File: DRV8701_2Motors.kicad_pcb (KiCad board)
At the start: 4 copper layers, 100 x 40 mm, 92 parts, among them J1 Conn_01x02, J10 Conn_01x04, J11 Conn_01x03, J2 Conn_01x10, J3 Conn_01x10, J4 Conn_01x02, J5 Conn_01x02, J6 Conn_01x04, J7 Conn_ST_STDC14, J8 Conn_01x03, J9 Conn_01x04, SW1 SW_SPDT_321, U16 STM32F303RETx, U3 AM26LV32xD, U4 AM26LV32xD

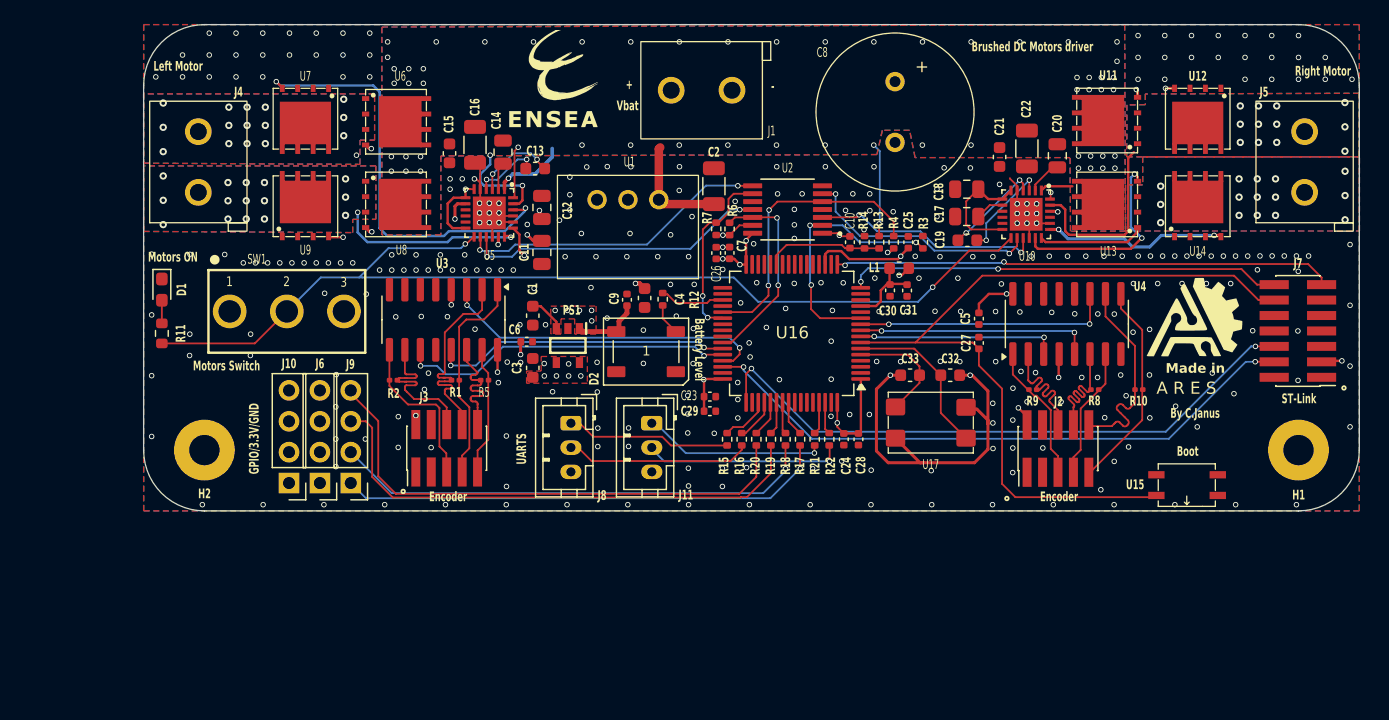
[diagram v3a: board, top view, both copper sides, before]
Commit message: V2 Driver-- avec control de courant
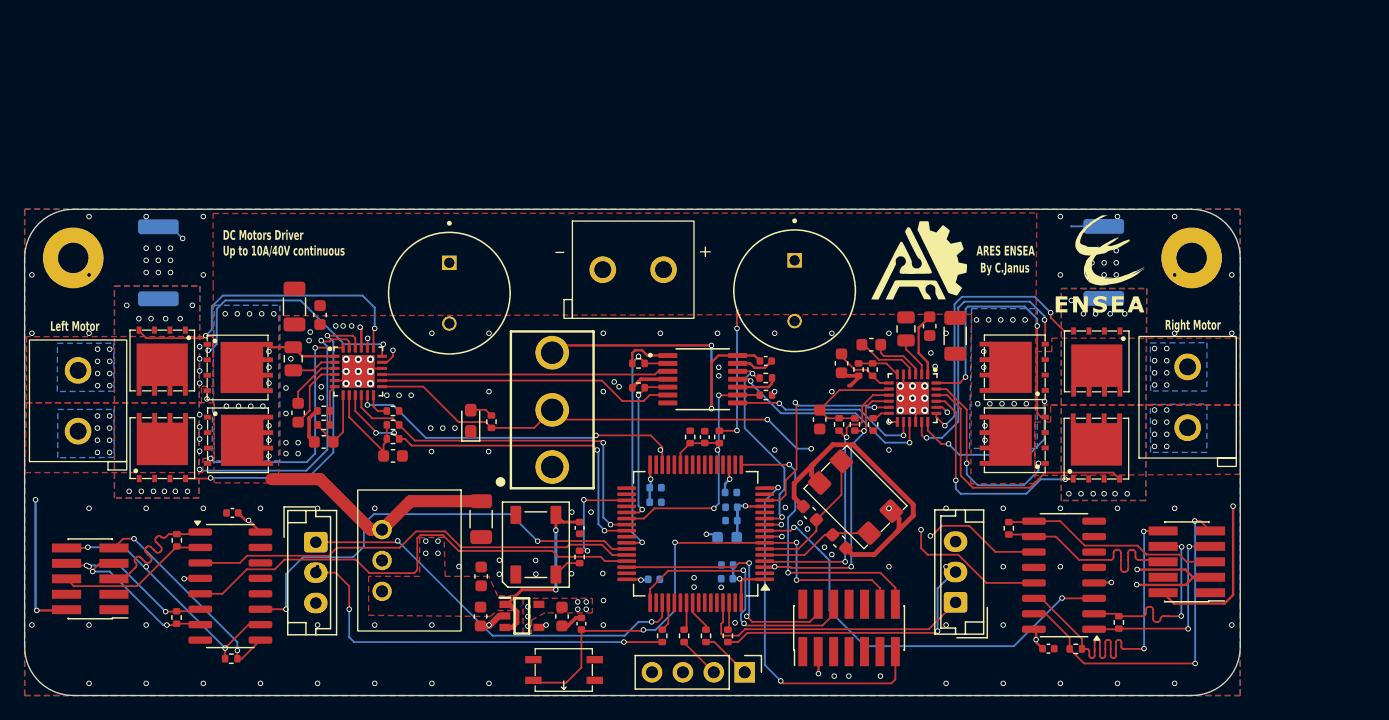
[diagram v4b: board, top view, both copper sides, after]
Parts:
- removed J10, J6: Conn_01x04, Connector_PinHeader_2.54mm:PinHeader_1x04_P2.54mm_Vertical
- removed J4, J5: Conn_01x02, KF301-5.0-2P:KF301-5.0-2P
- removed R15, R19, R20, R21: 220, Resistor_SMD:R_0402_1005Metric
- removed U11, U12, U13, U14, U6, U7, U8, U9: ~, TPH1R403NL:TPH1R403NL
- added C34: 220u, ECA1HHG471:ECA1HHG471, F.Cu at (109.0, 71.8)
- added J12: Conn_01x02, KF301-5.0-2P:KF301-5.0-2P, F.Cu at (169.7, 83.0)
- added J13: Conn_01x02, KF301-5.0-2P:KF301-5.0-2P, F.Cu at (78.4, 83.3)
- added R23: 3k3, Resistor_SMD:R_0402_1005Metric, F.Cu at (142.6, 78.2)
- added R24: 3k3, Resistor_SMD:R_0402_1005Metric, F.Cu at (98.6, 81.6)
- added R25: 2k, Resistor_SMD:R_0402_1005Metric, F.Cu at (143.8, 78.2)
- added R26: 2k, Resistor_SMD:R_0402_1005Metric, F.Cu at (98.6, 82.7)
- added R27: 10k, Resistor_SMD:R_0402_1005Metric, F.Cu at (141.0, 82.7)
- added R28: 10k, Resistor_SMD:R_0402_1005Metric, F.Cu at (104.3, 83.9)
- added R29: 10k, Resistor_SMD:R_0402_1005Metric, F.Cu at (142.3, 82.7)
- added R30: 10k, Resistor_SMD:R_0402_1005Metric, F.Cu at (104.3, 82.7)
- added R31: 33k, Resistor_SMD:R_0402_1005Metric, F.Cu at (143.8, 82.7)
- added R32: 33k, Resistor_SMD:R_0402_1005Metric, F.Cu at (104.3, 81.6)
- added R33: 50m, Resistor_SMD:R_2512_6332Metric, B.Cu at (162.8, 69.4)
- added R34: 50m, Resistor_SMD:R_2512_6332Metric, B.Cu at (85.0, 69.4)
- added U18: ~, TPH1R403NL:TPH1R403NL, F.Cu at (155.1, 84.0)
- added U19: ~, TPH1R403NL:TPH1R403NL, F.Cu at (91.9, 84.0)
- added U20: ~, TPH1R403NL:TPH1R403NL, F.Cu at (162.2, 84.3)
- added U21: ~, TPH1R403NL:TPH1R403NL, F.Cu at (85.3, 84.3)
- added U22: ~, TPH1R403NL:TPH1R403NL, F.Cu at (162.2, 77.9)
- added U23: ~, TPH1R403NL:TPH1R403NL, F.Cu at (85.3, 77.8)
- added U24: ~, TPH1R403NL:TPH1R403NL, F.Cu at (155.1, 78.0)
- added U25: ~, TPH1R403NL:TPH1R403NL, F.Cu at (91.9, 78.0)
- C11, C12, C17, C18: footprint Capacitor_SMD:C_0805_2012Metric -> Capacitor_SMD:C_0603_1608Metric
- C23, C24, C25, C26, C28, C29, C30, C31, L1: moved to B.Cu
- C8: value 470u -> 220u; footprint Capacitor:Wurth-470u-50V -> ECA1HHG471:ECA1HHG471
- J11, J8: footprint Connector_JST:JST_PH_B3B-PH-K_1x03_P2.00mm_Vertical -> Connector_JST:JST_EH_B3B-EH-A_1x03_P2.50mm_Vertical
- R1, R10, R2, R5, R8, R9: footprint Resistor_SMD:R_0201_0603Metric -> Resistor_SMD:R_0402_1005Metric
- R11: footprint Resistor_SMD:R_0603_1608Metric -> Resistor_SMD:R_0402_1005Metric
- R16, R22: value 220 -> 51
- moved H1 102.0 mm to (78.0, 69.0), turned to 0 degrees
- moved H2 82.7 mm to (170.0, 69.0), turned to 0 degrees
- moved J2 80.3 mm to (79.4, 95.4), turned to 180 degrees
- moved R10 77.9 mm to (91.0, 102.0)
- moved R8 77.8 mm to (86.5, 98.6), turned to -90 degrees
- moved U4 72.1 mm to (90.9, 96.0), turned to 0 degrees
- moved R9 71.5 mm to (86.5, 92.2), turned to 90 degrees
- moved C20 65.0 mm to (96.1, 77.3)
- moved C5 63.5 mm to (91.1, 90.0), turned to 180 degrees
- moved C22 61.6 mm to (96.2, 73.0)
- moved J3 61.6 mm to (169.6, 94.0), turned to 180 degrees
- moved R1 58.1 mm to (164.0, 99.0), turned to -90 degrees
- moved C21 57.4 mm to (98.3, 73.7)
- moved C19 56.8 mm to (96.5, 81.7), turned to -90 degrees
- moved U10 56.2 mm to (101.5, 78.4), turned to 0 degrees
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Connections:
- C11 pad 1: Net-(U5-DVDD) -> Net-(U5-AVDD)
- C12 pad 1: Net-(U5-AVDD) -> Net-(U10-AVDD)
- C17 pad 1: Net-(U10-DVDD) -> Net-(U5-DVDD)
- C18 pad 1: Net-(U10-AVDD) -> Net-(U10-DVDD)
- J11 pad 1: Net-(J11-Pin_1) -> /STM_et_Osc/Usart3_RX
- J7 pad 13: /STM_et_Osc/USART2_RX -> /STM_et_Osc/USART2_TX
- J7 pad 14: /STM_et_Osc/USART2_TX -> /STM_et_Osc/USART2_RX
- J8 pad 1: Net-(J8-Pin_1) -> /STM_et_Osc/Uart4_TX
- J9 pad 3: Net-(J9-Pin_3) -> +3.3V
- J9 pad 4: Net-(J9-Pin_4) -> GND
- U10 pad 10: unconnected-(U10-SNSOUT-Pad10) -> /L_nFAULT
- U10 pad 11: unconnected-(U10-SO-Pad11) -> /L_SO
- U10 pad 12: Net-(U10-AVDD) -> Net-(U10-IDRIVE)
- U10 pad 21: GND -> /MoteurGauche/Rsense
- U10 pad 22: /MoteurGauche/GL2 -> Net-(U10-GL2)
- U10 pad 24: /MoteurGauche/GH2 -> Net-(U10-GH2)
- U10 pad 6: Net-(U10-AVDD) -> Net-(U10-VREF)
- U10 pad 9: unconnected-(U10-nFAULT-Pad9) -> /L_SNSOUT
- U16 pad 10: /L_ENCI -> /R_ENCI
- U16 pad 11: /L_DIR_IN -> /R_DIR_IN
- U16 pad 14: unconnected-(U16-PA0-Pad14) -> /R_SO
- U16 pad 3: unconnected-(U16-PC14-Pad3) -> /R_SNSOUT
- U16 pad 30: unconnected-(U16-PB11-Pad30) -> /L_SO
- U16 pad 39: unconnected-(U16-PC8-Pad39) -> /L_nFAULT
- U16 pad 4: unconnected-(U16-PC15-Pad4) -> /R_nFAULT
- U16 pad 40: unconnected-(U16-PC9-Pad40) -> /L_SNSOUT
- U16 pad 42: /R_DIR_IN -> /L_DIR_IN
- U16 pad 43: /R_ENCI -> /L_ENCI
- U16 pad 44: /R_ENCA -> /L_ENCA
- U16 pad 45: /R_ENCB -> /L_ENCB
- U16 pad 53: /STM_et_Osc/PC12 -> unconnected-(U16-PC12-Pad53)
- U16 pad 54: /STM_et_Osc/PD2 -> unconnected-(U16-PD2-Pad54)
- U16 pad 8: /L_ENCA -> /R_ENCA
- U16 pad 9: /L_ENCB -> /R_ENCB
- U5 pad 10: unconnected-(U5-SNSOUT-Pad10) -> /R_SNSOUT
- U5 pad 11: unconnected-(U5-SO-Pad11) -> /R_SO
- U5 pad 12: Net-(U5-AVDD) -> Net-(U5-IDRIVE)
- U5 pad 21: GND -> /MoteurDroit/Rsense
- U5 pad 22: /MoteurDroit/GL2 -> Net-(U20-G)
- U5 pad 24: /MoteurDroit/GH2 -> Net-(U18-G)
- U5 pad 6: Net-(U5-AVDD) -> Net-(U5-VREF)
- U5 pad 9: unconnected-(U5-nFAULT-Pad9) -> /R_nFAULT
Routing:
- net GND: track 57.8 -> 119.7 mm, vias 326 -> 169
- net Net-(J9-Pin_4): track 42.9 -> 0.00 mm
- net Net-(J9-Pin_3): track 42.6 -> 0.00 mm
- net /nSLEEP: track 85.9 -> 47.2 mm, vias 2 -> 3
- net Net-(J9-Pin_2): track 40.0 -> 3.50 mm, vias 1 -> 0
- net Net-(J9-Pin_1): track 40.4 -> 4.21 mm, vias 1 -> 0
- net /MoteurDroit/GL2: track 35.3 -> 0.00 mm, vias 2 -> 0
- net /L_SNSOUT: track 0.00 -> 31.3 mm, vias 0 -> 4
- net /L_nFAULT: track 0.00 -> 30.4 mm, vias 0 -> 2
- net /STM_et_Osc/Uart4_TX: track 4.06 -> 33.6 mm, vias 0 -> 2
- net /STM_et_Osc/SWDIO: track 50.6 -> 21.8 mm
- net /STM_et_Osc/SWCLK: track 51.1 -> 22.8 mm
- net /L_SO: track 0.00 -> 28.1 mm, vias 0 -> 2
- net +5V: track 68.0 -> 41.7 mm, vias 8 -> 9
- net Net-(U10-GL2): track 0.00 -> 26.0 mm, vias 0 -> 2
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- added copper zone on B.Cu, net /MoteurDroit/Rsense
- added copper zone on F.Cu, net /MoteurDroit/Rsense
- added copper zone on B.Cu, net /MoteurGauche/Rsense
- added copper zone on F.Cu, net /MoteurGauche/Rsense
- added copper zone on In2.Cu, net /MoteurGauche/SH1
- added copper zone on In2.Cu, net /MoteurGauche/SH2
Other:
- outline, holes or cut-outs redrawn
- board text added: "ARES ENSEA"
- board text added: "DC Motors Driver Up to 10A/40V continuous"
- board text removed: "+"
- board text removed: "-"
- board text removed: "A R E S"
- board text removed: "Battery Level"
- board text removed: "Boot"
- board text removed: "Brushed DC Motors driver"
- board text removed: "Encoder"
- board text removed: "GPIO/3.3V/GND"
- board text removed: "Made in"
- board text removed: "Motors ON"
- board text removed: "Motors Switch"
- board text removed: "ST-Link"
- board text removed: "UARTS"
- board text removed: "Vbat"

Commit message: final push
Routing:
- net GND: track 119.7 -> 121.2 mm, vias 169 -> 257

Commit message: maj readme, supprimé deux vias non utiles
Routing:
- net GND: vias 257 -> 255
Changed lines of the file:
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@@
-	)
-	(via
-		(at 168.6 70.4)
-		(size 0.45)
-		(drill 0.3)
-		(layers "F.Cu" "B.Cu")
-		(free yes)
-		(net 1)
 	)
 	(via
@@
 		(size 0.45)
 		(drill 0.3)
-		(layers "F.Cu" "B.Cu")
-		(free yes)
-		(net 1)
-	)
-	(via
-		(at 79.3 70.4)
-		(size 0.45)
-		(drill 0.3)

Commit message: final push--tous les composants sur le Front
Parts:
- C23, C24, C25, C26, C28, C29, C30, C31, L1, R33, R34: moved to F.Cu
- moved G*** 71.4 mm to (90.7, 69.5)
- moved L1 9.34 mm to (134.9, 83.2), turned to 0 degrees
- moved C30 5.67 mm to (134.8, 85.6), turned to 0 degrees
- moved C31 5.67 mm to (134.8, 84.5), turned to 0 degrees
- moved C23 5.04 mm to (123.9, 84.5), turned to 180 degrees
- moved C25 4.71 mm to (135.7, 96.9), turned to 0 degrees
- moved C28 4.71 mm to (135.7, 98.0), turned to 0 degrees
- moved C26 4.51 mm to (132.4, 83.8), turned to -90 degrees
- moved C24 3.13 mm to (122.8, 96.5), turned to 180 degrees
- moved C29 3.11 mm to (123.9, 85.5), turned to 180 degrees
- moved R14 0.18 mm to (128.6, 83.8)
- moved C10 0.08 mm to (129.9, 83.8)
- moved R13 0.07 mm to (131.2, 83.8)
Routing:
- net GND: track 121.2 -> 116.8 mm, vias 255 -> 273
- net /MoteurDroit/SH2: track 15.9 -> 13.5 mm
- net /STM_et_Osc/USART2_RX: track 24.0 -> 21.7 mm
- net +3.3VA: track 5.93 -> 8.12 mm, vias 1 -> 0
- net /MoteurDroit/Rsense: track 18.6 -> 17.3 mm
- net VDC: track 42.7 -> 42.1 mm

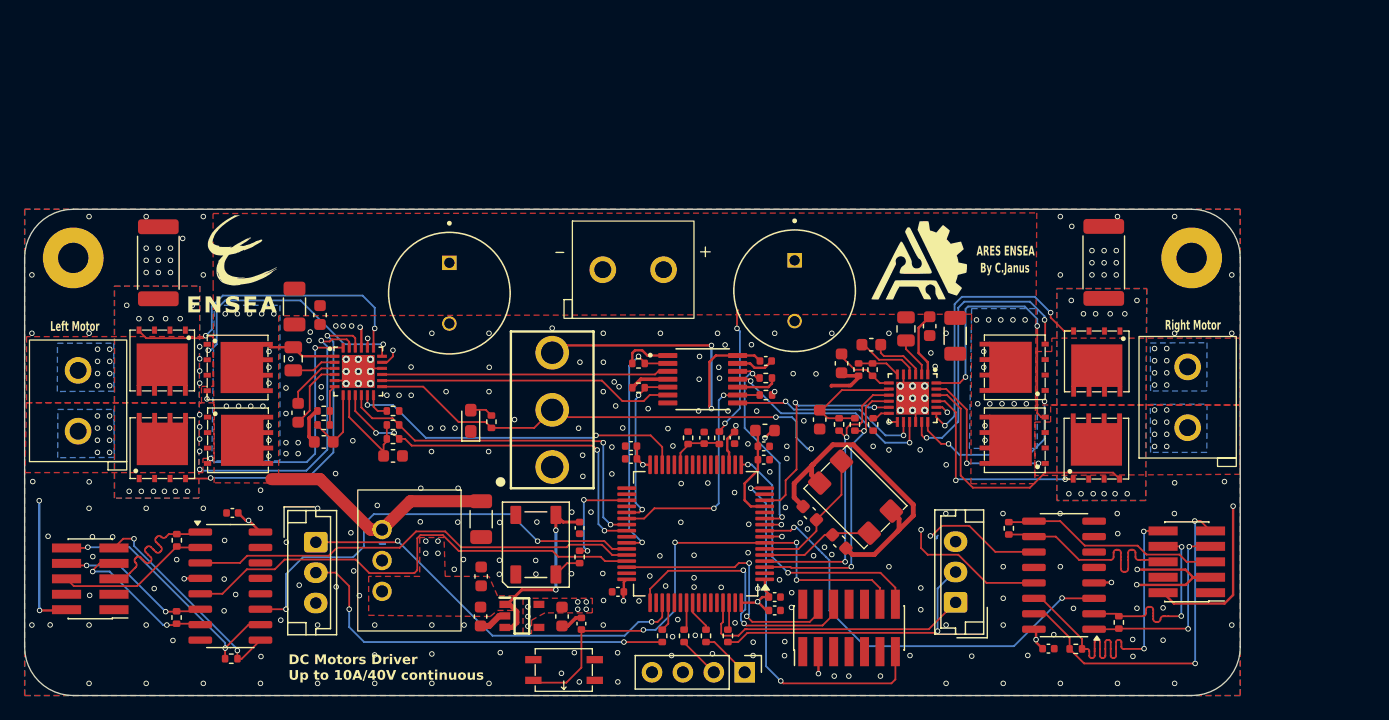
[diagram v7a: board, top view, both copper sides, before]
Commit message: alignement connecteur, changement connecteur
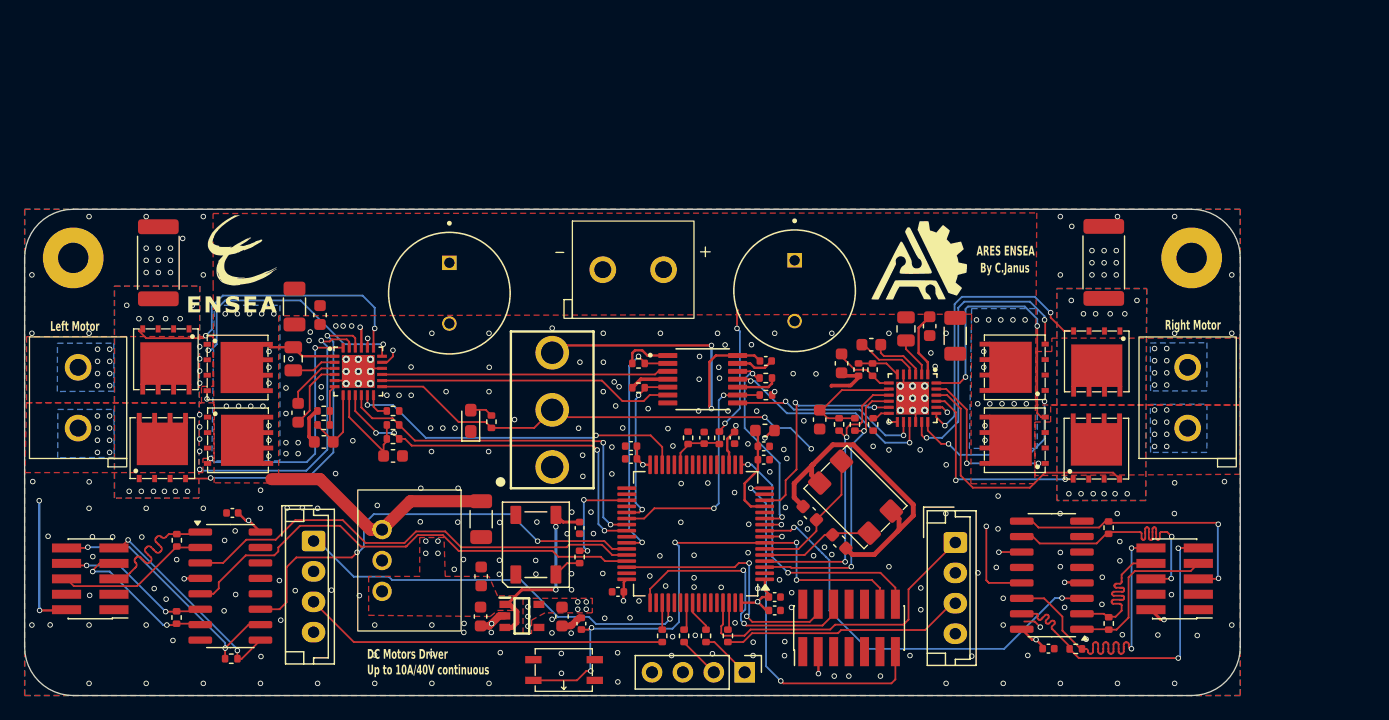
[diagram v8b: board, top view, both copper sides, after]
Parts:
- removed J11: Conn_01x03, Connector_JST:JST_EH_B3B-EH-A_1x03_P2.50mm_Vertical
- added J6: Conn_01x04, Connector_JST:JST_EH_B4B-EH-A_1x04_P2.50mm_Vertical, F.Cu at (97.8, 92.3)
- J8: value Conn_01x03 -> Conn_01x04; footprint Connector_JST:JST_EH_B3B-EH-A_1x03_P2.50mm_Vertical -> Connector_JST:JST_EH_B4B-EH-A_1x04_P2.50mm_Vertical
- moved J8 52.6 mm to (150.6, 92.4)
- moved R2 8.21 mm to (163.2, 91.2)
- moved J3 1.72 mm to (168.6, 95.4)
- moved U3 1.00 mm to (158.5, 95.1)
- moved R1 0.83 mm to (163.2, 99.1)
- moved U23 0.32 mm to (85.6, 77.7)
- moved J13 0.25 mm to (78.4, 83.0)
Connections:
- J8 pad 1: /STM_et_Osc/Uart4_TX -> /STM_et_Osc/Usart3_RX
- J8 pad 2: Net-(J8-Pin_2) -> GND
- J8 pad 3: GND -> Net-(J8-Pin_3)
- R16 pad 1: /STM_et_Osc/Uart4_RX -> /STM_et_Osc/Uart4_TX
- R16 pad 2: Net-(J8-Pin_2) -> Net-(J6-Pin_3)
- R22 pad 2: Net-(J11-Pin_2) -> Net-(J8-Pin_3)
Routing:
- net Net-(J8-Pin_2): track 32.8 -> 0.00 mm, vias 2 -> 0
- net /STM_et_Osc/Uart4_TX: track 33.6 -> 2.22 mm, vias 2 -> 0
- net /STM_et_Osc/Uart4_RX: track 2.42 -> 33.7 mm, vias 0 -> 1
- net Net-(J6-Pin_3): track 0.00 -> 30.1 mm
- net Net-(J11-Pin_2): track 23.2 -> 0.00 mm, vias 1 -> 0
- net Net-(J8-Pin_3): track 0.00 -> 20.0 mm
- net GND: track 116.8 -> 105.0 mm, vias 273 -> 284
- net /R_ChA: track 18.0 -> 23.0 mm, vias 0 -> 2
- net /R_ChA/: track 18.0 -> 22.9 mm, vias 0 -> 2
- net /STM_et_Osc/Usart3_RX: track 23.1 -> 26.5 mm
- net /R_ChI: track 30.3 -> 27.3 mm
- net /R_ChB/: track 16.3 -> 13.8 mm, vias 2 -> 0
- net /R_ChB: track 16.3 -> 13.8 mm, vias 2 -> 0
- net /STM_et_Osc/NRST: track 43.3 -> 45.3 mm, vias 4 -> 5
- net +5V: track 41.4 -> 43.4 mm
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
